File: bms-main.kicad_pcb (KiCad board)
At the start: 2 copper layers, 67 parts, among them J1 CONN HEADER VERT 2POS 1.5MM, J2 CONN HEADER VERT 2POS 1.5MM, J3 CONN HEADER VERT 2POS 1.5MM, J4 CONN HEADER VERT 4POS 2.5MM, J5 PIN HEADER 2.54MM PITCH STR D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, J6 XT60PW-M, J7 XT60PW-M, U1 TLE9015DQUXUMA1, U2 STM32L433CCU6, U3 IC TRANSCEIVER 1/1 8SO, U4 INA181A3IDBVR, X1 CRYSTAL 32.0000MHZ 10PF SMD

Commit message: 2 layer
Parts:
- C17, C20, R18: moved to B.Cu
- moved J1 22.3 mm to (143.5, 71.5), turned to -90 degrees
- moved J3 11.3 mm to (188.0, 43.5), turned to 90 degrees
- moved R2 9.13 mm to (173.7, 74.4)
- moved R3 9.13 mm to (171.7, 74.4)
- moved R4 9.13 mm to (169.7, 74.4)
- moved R8 9.06 mm to (167.9, 72.8)
- moved R9 8.86 mm to (166.1, 72.8)
- moved C17 8.60 mm to (167.0, 60.5), turned to 180 degrees
- moved J4 7.30 mm to (163.5, 38.1), turned to 180 degrees
- moved U1 6.80 mm to (170.7, 81.7)
- moved C1 6.80 mm to (163.5, 74.5)
- moved C3 6.80 mm to (163.5, 72.5)
- moved C4 6.80 mm to (160.0, 74.5)
- moved C5 6.80 mm to (164.0, 85.0)
- moved C6 6.80 mm to (163.5, 78.5)
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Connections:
- net /CANTranceiver/CANH_P renamed /CANTranceiver/CAN_P
- net /CANTranceiver/CANL_N renamed /CANTranceiver/CAN_N
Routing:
- net /STM/NRST: track 0.00 -> 31.5 mm, vias 0 -> 2
- net /isoUARTTranceiver/IFH_H: track 0.00 -> 19.7 mm
- net /isoUARTTranceiver/IFH_L: track 0.00 -> 17.9 mm
- net /CANTranceiver/STBY: track 0.00 -> 17.8 mm, vias 0 -> 2
- net /CANTranceiver/RXD: track 0.00 -> 17.6 mm
- net /STM/PB11/UART4_RX: track 0.00 -> 17.5 mm, vias 0 -> 2
- net /CANTranceiver/CAN_P: track 0.00 -> 16.2 mm
- net /CANTranceiver/TXD: track 0.00 -> 16.1 mm
- net /isoUARTTranceiver/ERRQ_RES: track 0.00 -> 16.0 mm
- net /isoUARTTranceiver/ERRQ_EXT: track 0.00 -> 15.9 mm
- net /STM/SWO: track 0.00 -> 15.6 mm, vias 0 -> 1
- net /CANTranceiver/CAN_N: track 0.00 -> 14.7 mm
- net /CurrentSense/C_Sense: track 0.00 -> 13.5 mm, vias 0 -> 2
- net /STM/SWDIO: track 0.00 -> 10.9 mm, vias 0 -> 1
- net /isoUARTTranceiver/UART_LS: track 0.00 -> 9.75 mm
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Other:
- board outline added: 49 x 53 mm

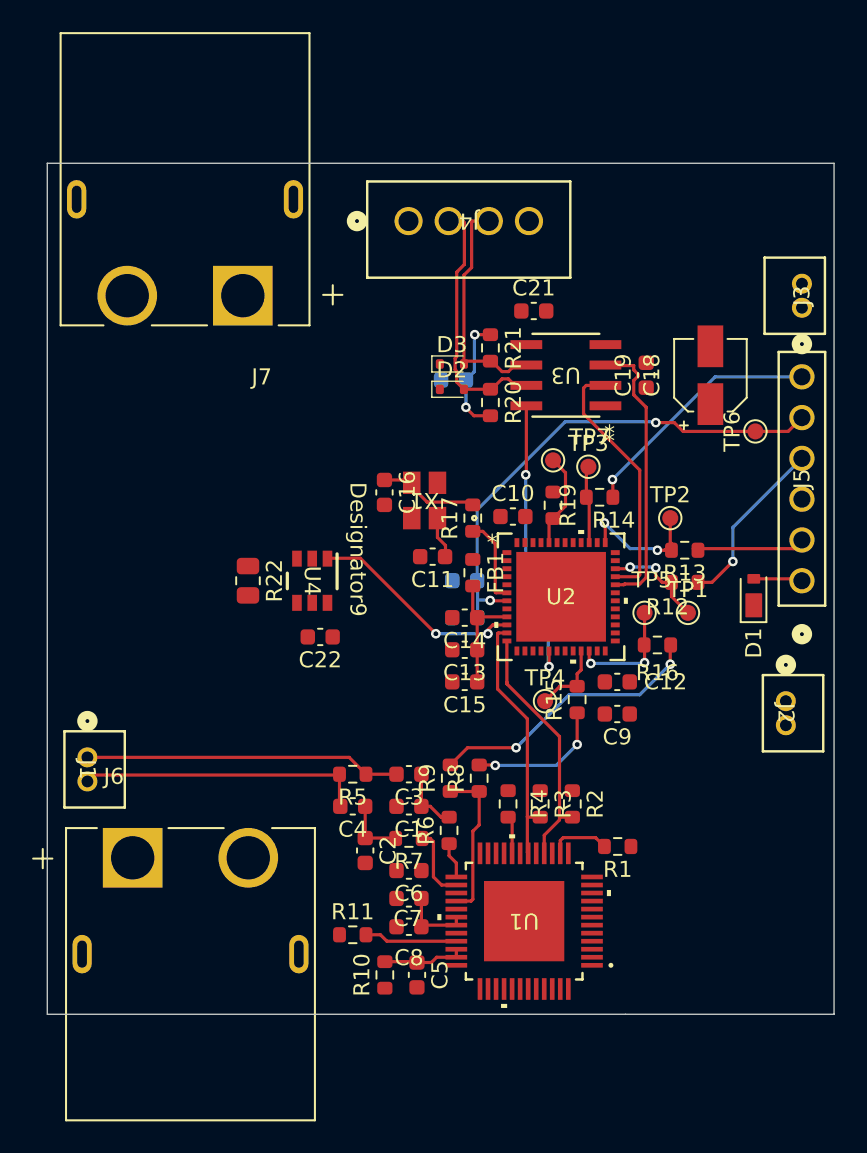
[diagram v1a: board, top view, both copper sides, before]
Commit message: switched to 4 layer and added traces
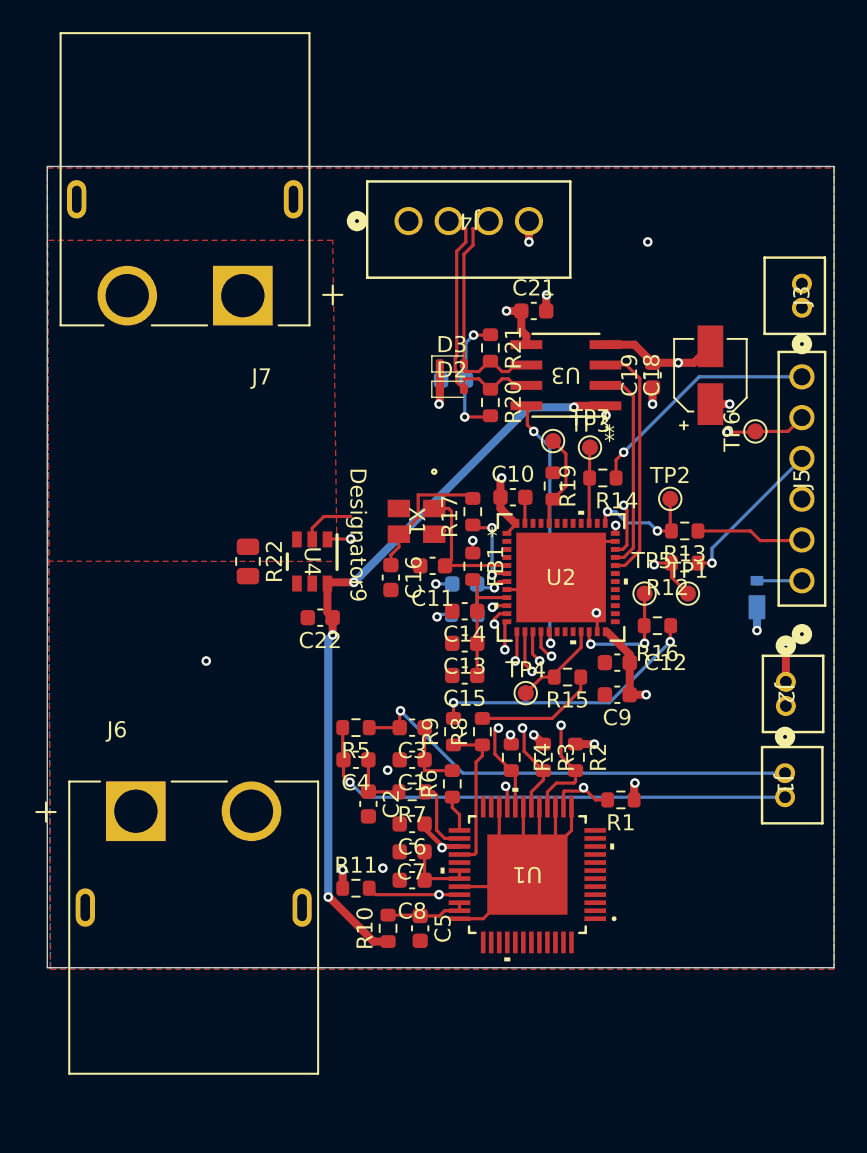
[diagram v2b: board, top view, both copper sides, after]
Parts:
- D1: moved to B.Cu
- moved J1 43.5 mm to (186.9, 72.5)
- moved C16 5.32 mm to (162.4, 60.3)
- moved R2 2.91 mm to (173.9, 71.5)
- moved R3 2.91 mm to (171.9, 71.5)
- moved R4 2.91 mm to (169.9, 71.5)
- moved U1 2.91 mm to (170.9, 78.8)
- moved R9 2.91 mm to (166.3, 69.9)
- moved C1 2.91 mm to (163.7, 71.7)
- moved C2 2.91 mm to (161.0, 74.4)
- moved C3 2.91 mm to (163.7, 69.7)
- moved C4 2.91 mm to (160.2, 71.7)
- moved C5 2.91 mm to (164.2, 82.2)
- moved C6 2.91 mm to (163.7, 75.7)
- moved C7 2.91 mm to (163.7, 77.4)
- moved C8 2.91 mm to (163.7, 79.2)
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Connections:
- J6 pad 1: BAT_GND -> GND
- J6 pad 2: BAT_GND -> GND
- J6 pad SH1: BAT_GND -> GND
- J6 pad SH2: BAT_GND -> GND
- J7 pad SH1: BAT_GND -> GND
- J7 pad SH2: BAT_GND -> GND
- R22 pad 2: BAT_GND -> GND
- U4 pad 4: BAT_GND -> GND
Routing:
- net GND: track 0.00 -> 66.2 mm, vias 0 -> 10
- net 5V: track 0.00 -> 49.7 mm, vias 0 -> 7
- net 3V3: track 0.00 -> 27.5 mm, vias 0 -> 14
- net /STM/PA6/ERRQ: track 5.79 -> 25.4 mm, vias 0 -> 2
- net /isoUARTTranceiver/IFH_L: track 17.9 -> 31.1 mm, vias 0 -> 1
- net /STM/PA5/ERR_loc_OUT: track 0.00 -> 12.2 mm, vias 0 -> 2
- net /isoUARTTranceiver/NSLEEP: track 3.85 -> 15.6 mm, vias 0 -> 2
- net /isoUARTTranceiver/ERR_EXT_OUT: track 2.35 -> 12.8 mm, vias 0 -> 2
- net /isoUARTTranceiver/IFH_H: track 19.7 -> 28.5 mm, vias 0 -> 1
- net /STM/PH0-OSC_IN: track 2.62 -> 8.57 mm
- net /STM/SWDIO/PA13: track 6.55 -> 11.3 mm
- net /STM/NRST: track 31.5 -> 27.7 mm
- net /CANTranceiver/TXD: track 16.1 -> 12.8 mm
- net /CANTranceiver/RXD: track 17.6 -> 15.1 mm
- net Net-(C16-Pad1): track 6.29 -> 8.66 mm
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- added copper zone on In1.Cu, net 3V3
- added copper zone on In1.Cu, net 5V
- added copper zone on B.Cu, net GND
- added copper zone on F.Cu, net GND
- added copper zone on In1.Cu, net GND
- added copper zone on In2.Cu, net GND
- added copper zone on F.Cu, net PD_GND
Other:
- board size 49 x 53 mm -> 49 x 49.9 mm
- copper layers 2 -> 4

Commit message: layout review
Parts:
- moved J2 8.58 mm to (187.0, 75.4)
- moved J1 3.86 mm to (188.1, 68.8), turned to 90 degrees
- moved R17 3.52 mm to (167.1, 59.7), turned to 180 degrees
- moved C11 3.45 mm to (167.4, 57.1), turned to -90 degrees
- moved FB1 1.90 mm to (167.0, 61.4), turned to 0 degrees
- moved C16 1.33 mm to (163.7, 60.0), turned to 0 degrees
- moved J3 1.20 mm to (188.1, 42.3)
- moved C14 0.93 mm to (167.0, 63.3)
- moved C13 0.70 mm to (167.0, 65.1)
- moved C15 0.50 mm to (167.0, 66.9)
- moved SWCLK 0.40 mm to (180.2, 55.4)
- moved R13 0.30 mm to (181.0, 57.4)
- moved X1 0.20 mm to (164.0, 57.0)
- renumbered TP7 to BOOT, TP6 to NRST, TP2 to SWCLK, TP1 to SWDIO, TP3 to SWO, TP5 to UARTTX
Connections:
- net /isoUARTTranceiver/IFH_H renamed /isoUARTTranceiver/IFH_P
- net /isoUARTTranceiver/IFH_H_Filt renamed /isoUARTTranceiver/IFH_Filt_P
- net /isoUARTTranceiver/IFH_L renamed /isoUARTTranceiver/IFH_N
- net /isoUARTTranceiver/IFH_L_Filt renamed /isoUARTTranceiver/IFH_Filt_N
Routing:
- net GND: track 66.2 -> 71.8 mm
- net /STM/SWDIO/PA13: track 11.3 -> 6.26 mm
- net /STM/PH1-OSC_OUT: track 5.26 -> 1.84 mm, vias 2 -> 0
- net PD_GND: track 0.00 -> 3.24 mm
- net /isoUARTTranceiver/IFH_P: track 28.5 -> 31.5 mm
- net Net-(C16-Pad1): track 8.66 -> 6.50 mm
- net /isoUARTTranceiver/IFH_N: track 31.1 -> 32.8 mm
- net Net-(U2B-VDDA/VREF+): track 8.42 -> 6.77 mm
- net /CANTranceiver/RXD: track 15.1 -> 16.4 mm
- net /CANTranceiver/TXD: track 12.8 -> 14.2 mm
- net /STM/PH0-OSC_IN: track 8.57 -> 7.26 mm
- net 3V3: track 27.5 -> 26.3 mm, vias 14 -> 12

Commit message: layout silkscreens/labels fixed tps added
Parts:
- added CANN: TestPoint, TestPoint:TestPoint_Pad_D1.0mm, F.Cu at (175.4, 40.7)
- added CANP: TestPoint, TestPoint:TestPoint_Pad_D1.0mm, F.Cu at (175.4, 38.0)
- R9: value 0 -> RES 0 OHM JUMPER 1/10W 0603
- renumbered UARTTX to URX, TP4 to UTX
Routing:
- net /CANTranceiver/CAN_P: track 17.0 -> 30.0 mm
- net /CANTranceiver/CAN_N: track 14.9 -> 24.8 mm
- added copper zone on B.Cu, net PD_GND
- added copper zone on In1.Cu, net PD_GND
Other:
- board text added: "3V3"
- board text added: "5V"
- board text added: "AFE"
- board text added: "CAN"
- board text added: "JTAG"

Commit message: fixed minor layout
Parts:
- moved UTX 0.86 mm to (170.3, 66.8)
- moved C22 0.22 mm to (157.8, 62.7)
- moved R15 0.20 mm to (173.2, 66.5)
- moved J2 0.10 mm to (187.1, 75.4)
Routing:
- net /STM/SWCLK/PA14: track 7.44 -> 6.51 mm
- net /STM/USART4_TX: track 5.71 -> 6.43 mm
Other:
- board text added: "BAT GND"
- board text added: "GND"

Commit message: damir review fix
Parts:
- moved CANP 10.8 mm to (166.0, 43.3)
- moved N 7.66 mm to (168.2, 43.3)
- moved C11 3.28 mm to (165.7, 54.3), turned to 180 degrees
- moved R10 1.93 mm to (163.9, 81.2), turned to 0 degrees
- moved X1 1.60 mm to (165.6, 56.9)
- moved C5 1.50 mm to (165.3, 83.2), turned to 0 degrees
- moved UTX 0.42 mm to (170.6, 67.1)
- moved C16 0.32 mm to (163.8, 59.7), turned to 180 degrees
- moved C14 0.20 mm to (167.2, 63.3)
- moved C13 0.20 mm to (167.2, 65.1)
- moved C15 0.20 mm to (167.2, 66.9)
- moved C8 0.18 mm to (163.9, 79.2)
- moved FB1 0.10 mm to (167.1, 61.4)
- moved C6 0.09 mm to (163.8, 75.7)
- moved C7 0.08 mm to (163.8, 77.4)
- renumbered CANN to N
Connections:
- X1 pad 2: unconnected-(X1-Pad2) -> GND
- X1 pad 4: unconnected-(X1-Pad4) -> GND
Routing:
- net /CANTranceiver/CAN_P: track 30.0 -> 17.8 mm
- net /CANTranceiver/CAN_N: track 24.8 -> 16.7 mm
- net Net-(C16-Pad1): track 6.50 -> 0.14 mm
- net 3V3: track 26.5 -> 31.5 mm
- net Net-(U2B-VDDA/VREF+): track 6.77 -> 1.87 mm
- net 5V: track 49.4 -> 54.0 mm, vias 7 -> 9
- net GND: track 71.8 -> 74.8 mm, vias 10 -> 11
- net /STM/PH0-OSC_IN: track 7.26 -> 5.41 mm
- net PD_GND: track 3.24 -> 4.56 mm
- net Net-(U1-VIO): track 4.48 -> 5.74 mm
- net /CANTranceiver/STBY: track 16.2 -> 17.3 mm
- net /STM/PB10/UART3_TX: track 7.98 -> 7.27 mm
- added copper zone on F.Cu, net /STM/PH0-OSC_IN
- added copper zone on F.Cu, net Net-(C16-Pad1)
- added copper zone on F.Cu, net Net-(C5-Pad1)
- added copper zone on F.Cu, net Net-(U1-VIO)
- added copper zone on F.Cu, net Net-(U2B-VDDA/VREF+)
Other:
- board text added: "CANN"
- board text added: "CANP"
- board text added: "IFHN"
- board text added: "IFHP"
- board text removed: "CAN"

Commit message: minor changes
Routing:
- net PD_GND: vias 0 -> 20
- net GND: vias 11 -> 58

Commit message: minor fixes
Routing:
- net 5V: track 54.0 -> 50.7 mm
- net GND: track 74.8 -> 73.5 mm, vias 58 -> 57
- net 3V3: track 31.5 -> 30.9 mm
- added copper zone on F.Cu, net 5V
